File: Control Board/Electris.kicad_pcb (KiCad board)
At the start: 2 copper layers, 57 parts, among them J1 Barrel_Jack, J2 CTRL_ICSP, J3 GFX_ICSP, J4 VGA, Q1 MMBT2222ALT3G, SW1 SW_ML, SW2 SW_MR, SW3 SW_TL, SW4 SW_TR, SW5 SW_DS, SW6 SW_DH, SW7 SW_HL, U1 ATmega328P-AU, U2 AP1509-50SG-13, U3 ATmega328P-AU, Y1 16MHz, Y2 16MHz

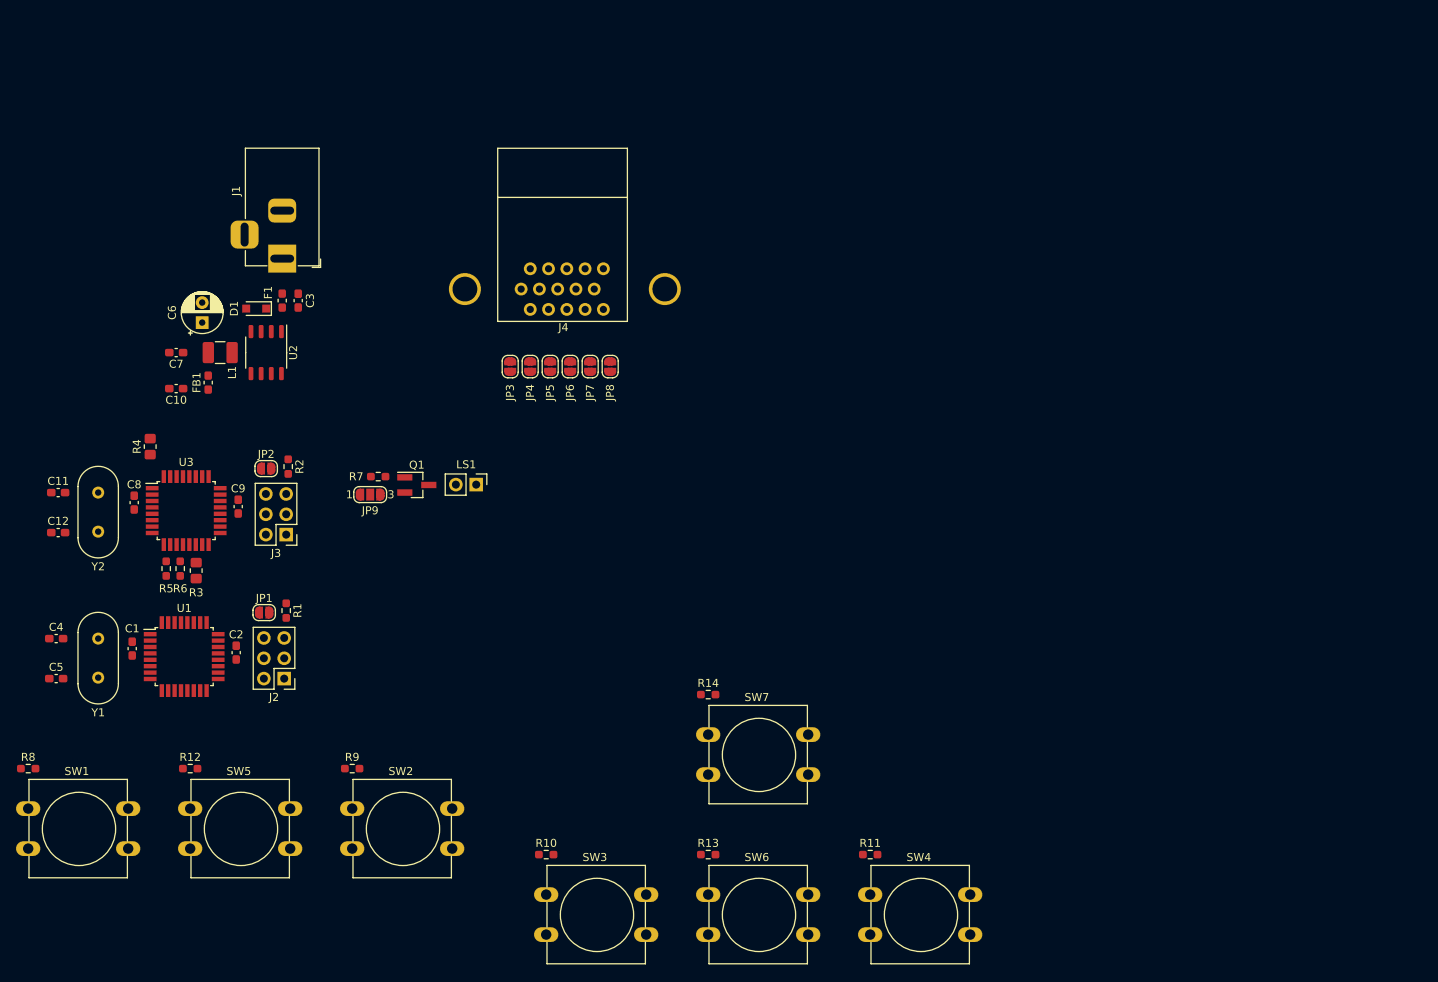
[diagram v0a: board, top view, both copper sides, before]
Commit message: Switched to RP2040, finished schematic, started layout.
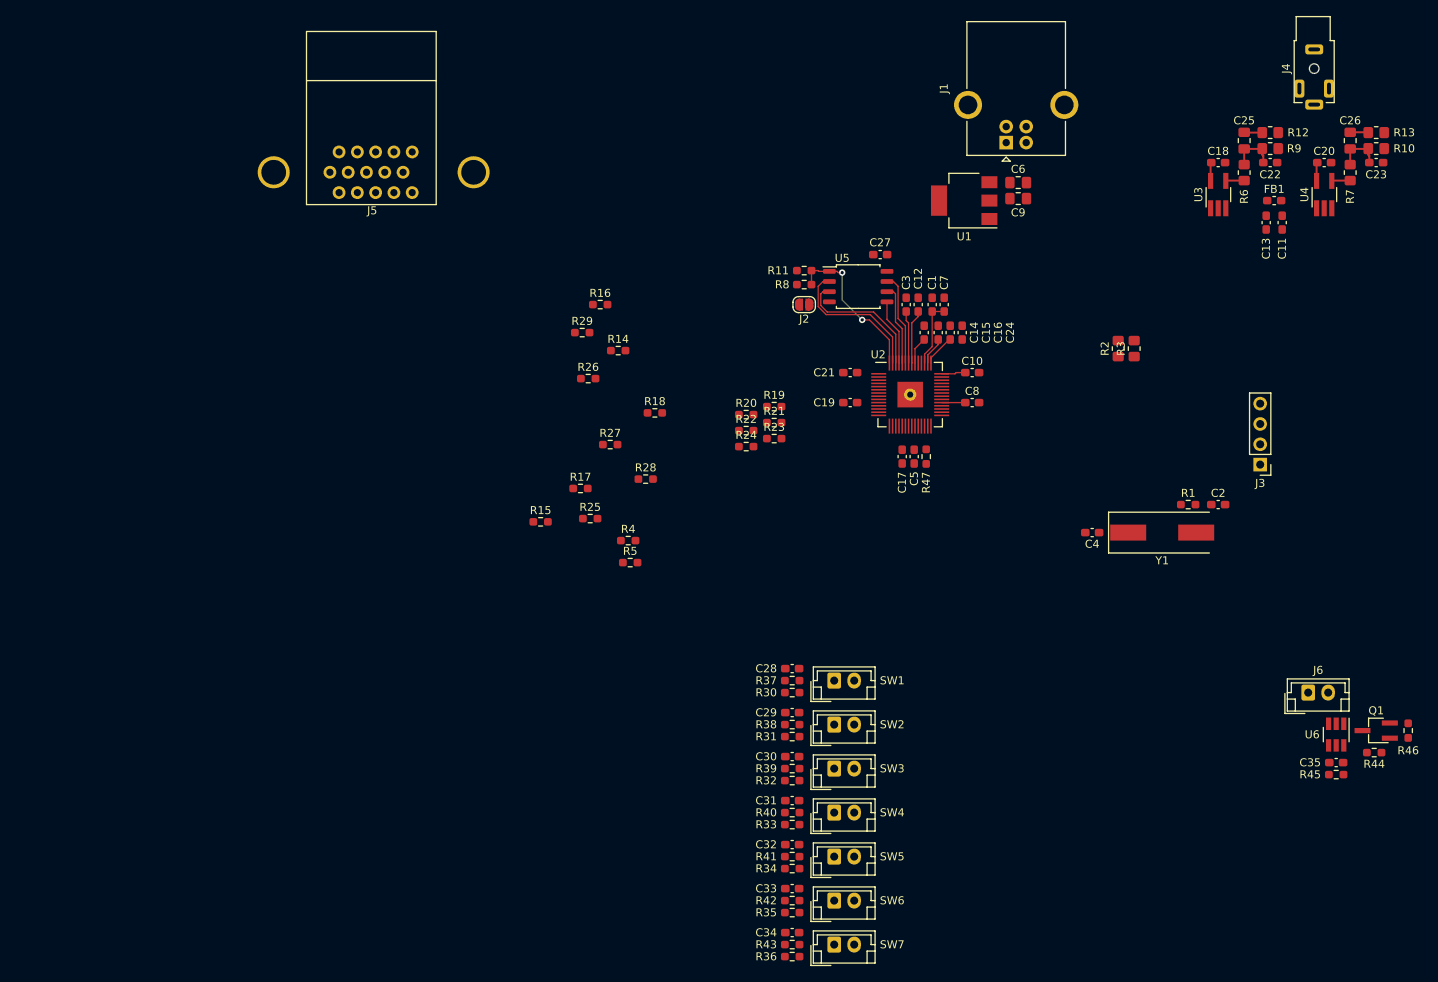
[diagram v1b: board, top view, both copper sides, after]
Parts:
- removed D1: NSR0530HT1G, Diode_SMD:D_SOD-323_HandSoldering
- removed F1: 500mA, Fuse:Fuse_0603_1608Metric_Pad1.05x0.95mm_HandSolder
- removed JP1: CTRL_RST, Jumper:SolderJumper-2_P1.3mm_Open_RoundedPad1.0x1.5mm
- removed JP2: GFX_RST, Jumper:SolderJumper-2_P1.3mm_Open_RoundedPad1.0x1.5mm
- removed JP3: 6R, Jumper:SolderJumper-2_P1.3mm_Open_RoundedPad1.0x1.5mm
- removed JP4: 6G, Jumper:SolderJumper-2_P1.3mm_Open_RoundedPad1.0x1.5mm
- removed JP5: 6B, Jumper:SolderJumper-2_P1.3mm_Open_RoundedPad1.0x1.5mm
- removed JP6: 7R, Jumper:SolderJumper-2_P1.3mm_Open_RoundedPad1.0x1.5mm
- removed JP7: 7G, Jumper:SolderJumper-2_P1.3mm_Open_RoundedPad1.0x1.5mm
- removed JP8: 7B, Jumper:SolderJumper-2_P1.3mm_Open_RoundedPad1.0x1.5mm
- removed JP9: TONE, Jumper:SolderJumper-3_P1.3mm_Open_RoundedPad1.0x1.5mm_NumberLabels
- removed L1: 47uH, Inductor_SMD:L_1210_3225Metric_Pad1.42x2.65mm_HandSolder
- removed LS1: Speaker, Connector_PinHeader_2.54mm:PinHeader_1x02_P2.54mm_Vertical
- removed Y2: 16MHz, Crystal:Crystal_HC49-4H_Vertical
- added C13: 0.1uF, Capacitor_SMD:C_0603_1608Metric_Pad1.08x0.95mm_HandSolder, F.Cu at (230.8, 54.2)
- added C14: 0.1uF, Capacitor_SMD:C_0603_1608Metric_Pad1.08x0.95mm_HandSolder, F.Cu at (188.0, 68.0)
- added C15: 0.1uF, Capacitor_SMD:C_0603_1608Metric_Pad1.08x0.95mm_HandSolder, F.Cu at (189.8, 68.0)
- added C16: 0.1uF, Capacitor_SMD:C_0603_1608Metric_Pad1.08x0.95mm_HandSolder, F.Cu at (191.2, 68.0)
- added C17: 0.1uF, Capacitor_SMD:C_0603_1608Metric_Pad1.08x0.95mm_HandSolder, F.Cu at (185.2, 83.5)
- added C18: 0.1uF, Capacitor_SMD:C_0603_1608Metric_Pad1.08x0.95mm_HandSolder, F.Cu at (224.8, 46.8)
- added C19: 0.1uF, Capacitor_SMD:C_0603_1608Metric_Pad1.08x0.95mm_HandSolder, F.Cu at (178.8, 76.8)
- added C20: 0.1uF, Capacitor_SMD:C_0603_1608Metric_Pad1.08x0.95mm_HandSolder, F.Cu at (238.0, 46.8)
- added C21: 0.1uF, Capacitor_SMD:C_0603_1608Metric_Pad1.08x0.95mm_HandSolder, F.Cu at (178.8, 73.0)
- added C22: 0.1uF, Capacitor_SMD:C_0603_1608Metric_Pad1.08x0.95mm_HandSolder, F.Cu at (231.2, 46.8)
- added C23: 0.1uF, Capacitor_SMD:C_0603_1608Metric_Pad1.08x0.95mm_HandSolder, F.Cu at (244.5, 46.8)
- added C24: 1uF, Capacitor_SMD:C_0603_1608Metric_Pad1.08x0.95mm_HandSolder, F.Cu at (192.8, 68.0)
- added C25: 47uF, Capacitor_SMD:C_0805_2012Metric_Pad1.18x1.45mm_HandSolder, F.Cu at (228.0, 44.0)
- added C26: 47uF, Capacitor_SMD:C_0805_2012Metric_Pad1.18x1.45mm_HandSolder, F.Cu at (241.2, 44.0)
- added C27: 0.1uF, Capacitor_SMD:C_0603_1608Metric_Pad1.08x0.95mm_HandSolder, F.Cu at (182.5, 58.2)
- added C28: 0.1uF, Capacitor_SMD:C_0603_1608Metric_Pad1.08x0.95mm_HandSolder, F.Cu at (171.5, 110.0)
- added C29: 0.1uF, Capacitor_SMD:C_0603_1608Metric_Pad1.08x0.95mm_HandSolder, F.Cu at (171.5, 115.5)
- added C30: 0.1uF, Capacitor_SMD:C_0603_1608Metric_Pad1.08x0.95mm_HandSolder, F.Cu at (171.5, 121.0)
- added C31: 0.1uF, Capacitor_SMD:C_0603_1608Metric_Pad1.08x0.95mm_HandSolder, F.Cu at (171.5, 126.5)
- added C32: 0.1uF, Capacitor_SMD:C_0603_1608Metric_Pad1.08x0.95mm_HandSolder, F.Cu at (171.5, 132.0)
- added C33: 0.1uF, Capacitor_SMD:C_0603_1608Metric_Pad1.08x0.95mm_HandSolder, F.Cu at (171.5, 137.5)
- added C34: 0.1uF, Capacitor_SMD:C_0603_1608Metric_Pad1.08x0.95mm_HandSolder, F.Cu at (171.5, 143.0)
- added C35: 1uF, Capacitor_SMD:C_0603_1608Metric_Pad1.08x0.95mm_HandSolder, F.Cu at (239.5, 121.8)
- added J5: VGA, jlib:Connector_Amphenol_ICD15S13E4GX00LF, F.Cu at (124.0, 50.5)
- added J6: LED_1, Connector_JST:JST_EH_B2B-EH-A_1x02_P2.50mm_Vertical, F.Cu at (236.0, 113.0)
- added R15: 1K, Resistor_SMD:R_0603_1608Metric_Pad0.98x0.95mm_HandSolder, F.Cu at (140.1, 91.7)
- added R16: 2K, Resistor_SMD:R_0603_1608Metric_Pad0.98x0.95mm_HandSolder, F.Cu at (147.5, 64.5)
- added R17: 4.02K, Resistor_SMD:R_0603_1608Metric_Pad0.98x0.95mm_HandSolder, F.Cu at (145.0, 87.5)
- added R18: 8.06K, Resistor_SMD:R_0603_1608Metric_Pad0.98x0.95mm_HandSolder, F.Cu at (154.3, 78.0)
- added R19: 499, Resistor_SMD:R_0603_1608Metric_Pad0.98x0.95mm_HandSolder, F.Cu at (169.2, 77.2)
- added R20: 1K, Resistor_SMD:R_0603_1608Metric_Pad0.98x0.95mm_HandSolder, F.Cu at (165.8, 78.2)
- added R21: 2K, Resistor_SMD:R_0603_1608Metric_Pad0.98x0.95mm_HandSolder, F.Cu at (169.2, 79.2)
- added R22: 4.02K, Resistor_SMD:R_0603_1608Metric_Pad0.98x0.95mm_HandSolder, F.Cu at (165.8, 80.2)
- added R23: 8.06K, Resistor_SMD:R_0603_1608Metric_Pad0.98x0.95mm_HandSolder, F.Cu at (169.2, 81.2)
- added R24: 16K, Resistor_SMD:R_0603_1608Metric_Pad0.98x0.95mm_HandSolder, F.Cu at (165.8, 82.2)
- added R25: 499, Resistor_SMD:R_0603_1608Metric_Pad0.98x0.95mm_HandSolder, F.Cu at (146.2, 91.2)
- added R26: 1K, Resistor_SMD:R_0603_1608Metric_Pad0.98x0.95mm_HandSolder, F.Cu at (146.0, 73.8)
- added R27: 2K, Resistor_SMD:R_0603_1608Metric_Pad0.98x0.95mm_HandSolder, F.Cu at (148.8, 82.0)
- added R28: 4.02K, Resistor_SMD:R_0603_1608Metric_Pad0.98x0.95mm_HandSolder, F.Cu at (153.2, 86.3)
- added R29: 8.06K, Resistor_SMD:R_0603_1608Metric_Pad0.98x0.95mm_HandSolder, F.Cu at (145.2, 68.0)
- added R30: 10K, Resistor_SMD:R_0603_1608Metric_Pad0.98x0.95mm_HandSolder, F.Cu at (171.5, 113.0)
- added R31: 10K, Resistor_SMD:R_0603_1608Metric_Pad0.98x0.95mm_HandSolder, F.Cu at (171.5, 118.5)
- added R32: 10K, Resistor_SMD:R_0603_1608Metric_Pad0.98x0.95mm_HandSolder, F.Cu at (171.5, 124.0)
- added R33: 10K, Resistor_SMD:R_0603_1608Metric_Pad0.98x0.95mm_HandSolder, F.Cu at (171.5, 129.5)
- added R34: 10K, Resistor_SMD:R_0603_1608Metric_Pad0.98x0.95mm_HandSolder, F.Cu at (171.5, 135.0)
- added R35: 10K, Resistor_SMD:R_0603_1608Metric_Pad0.98x0.95mm_HandSolder, F.Cu at (171.5, 140.5)
- added R36: 10K, Resistor_SMD:R_0603_1608Metric_Pad0.98x0.95mm_HandSolder, F.Cu at (171.5, 146.0)
- added R37: 1K, Resistor_SMD:R_0603_1608Metric_Pad0.98x0.95mm_HandSolder, F.Cu at (171.5, 111.5)
- added R38: 1K, Resistor_SMD:R_0603_1608Metric_Pad0.98x0.95mm_HandSolder, F.Cu at (171.5, 117.0)
- added R39: 1K, Resistor_SMD:R_0603_1608Metric_Pad0.98x0.95mm_HandSolder, F.Cu at (171.5, 122.5)
- added R40: 1K, Resistor_SMD:R_0603_1608Metric_Pad0.98x0.95mm_HandSolder, F.Cu at (171.5, 128.0)
- added R41: 1K, Resistor_SMD:R_0603_1608Metric_Pad0.98x0.95mm_HandSolder, F.Cu at (171.5, 133.5)
- added R42: 1K, Resistor_SMD:R_0603_1608Metric_Pad0.98x0.95mm_HandSolder, F.Cu at (171.5, 139.0)
- added R43: 1K, Resistor_SMD:R_0603_1608Metric_Pad0.98x0.95mm_HandSolder, F.Cu at (171.5, 144.5)
- added R44: 1K, Resistor_SMD:R_0603_1608Metric_Pad0.98x0.95mm_HandSolder, F.Cu at (244.2, 120.5)
- added R45: 10K, Resistor_SMD:R_0603_1608Metric_Pad0.98x0.95mm_HandSolder, F.Cu at (239.5, 123.2)
- added R46: 10K, Resistor_SMD:R_0603_1608Metric_Pad0.98x0.95mm_HandSolder, F.Cu at (248.5, 117.8)
- added R47: 10K, Resistor_SMD:R_0603_1608Metric_Pad0.98x0.95mm_HandSolder, F.Cu at (188.2, 83.5)
- added U4: 74LVC1G17, Package_TO_SOT_SMD:TSOT-23-5_HandSoldering, F.Cu at (238.0, 50.8)
- added U5: W25Q128JVS, Package_SO:SOIC-8_5.23x5.23mm_P1.27mm, F.Cu at (179.8, 62.2)
- added U6: BCR401UW6Q, Package_TO_SOT_SMD:SOT-23-6_Handsoldering, F.Cu at (239.5, 118.2)
- C11, C12, C5: value 18pF -> 0.1uF
- C2: value 0.1uF -> 27pF
- C4: value 18pF -> 27pF
- C6: value 47uF -> 10uF; footprint Capacitor_THT:CP_Radial_D5.0mm_P2.50mm -> Capacitor_SMD:C_0805_2012Metric_Pad1.18x1.45mm_HandSolder
- C7: value 0.1uF -> 1uF
- C9: value 0.1uF -> 10uF; footprint Capacitor_SMD:C_0603_1608Metric_Pad1.08x0.95mm_HandSolder -> Capacitor_SMD:C_0805_2012Metric_Pad1.18x1.45mm_HandSolder
- FB1: value Ferrite -> FERRITE
- J1: value Barrel_Jack -> USB; footprint Connector_BarrelJack:BarrelJack_Horizontal -> Connector_USB:USB_B_OST_USB-B1HSxx_Horizontal
- J2: value CTRL_ICSP -> USB_BOOT; footprint Connector_PinHeader_2.54mm:PinHeader_2x03_P2.54mm_Vertical -> Jumper:SolderJumper-2_P1.3mm_Open_RoundedPad1.0x1.5mm
- J3: value GFX_ICSP -> SWD; footprint Connector_PinHeader_2.54mm:PinHeader_2x03_P2.54mm_Vertical -> Connector_PinHeader_2.54mm:PinHeader_1x04_P2.54mm_Vertical
- J4: value VGA -> AUDIO; footprint jlib:Connector_Amphenol_ICD15S13E4GX00LF -> jlib:Connector_CUI_SJ1-2503A
- Q1: footprint Package_TO_SOT_SMD:SOT-23_Handsoldering -> Package_TO_SOT_SMD:TSOT-23_HandSoldering
- R1, R8: value 10K -> 1K
- R10, R9: value 10K -> 100; footprint Resistor_SMD:R_0603_1608Metric_Pad0.98x0.95mm_HandSolder -> Resistor_SMD:R_0805_2012Metric_Pad1.20x1.40mm_HandSolder
- R11: value 10K -> DNP
- R12, R13: value 10K -> 1.8K; footprint Resistor_SMD:R_0603_1608Metric_Pad0.98x0.95mm_HandSolder -> Resistor_SMD:R_0805_2012Metric_Pad1.20x1.40mm_HandSolder
- R14: value 10K -> 499
- R2: value 10K -> 27K; footprint Resistor_SMD:R_0603_1608Metric_Pad0.98x0.95mm_HandSolder -> Resistor_SMD:R_0805_2012Metric_Pad1.20x1.40mm_HandSolder
- R3: value 68 -> 27K
- R4: value 68 -> 47; footprint Resistor_SMD:R_0805_2012Metric_Pad1.20x1.40mm_HandSolder -> Resistor_SMD:R_0603_1608Metric_Pad0.98x0.95mm_HandSolder
- R5: value 470 -> 47
- R6: value 470 -> 220; footprint Resistor_SMD:R_0603_1608Metric_Pad0.98x0.95mm_HandSolder -> Resistor_SMD:R_0805_2012Metric_Pad1.20x1.40mm_HandSolder
- R7: value 1K -> 220; footprint Resistor_SMD:R_0603_1608Metric_Pad0.98x0.95mm_HandSolder -> Resistor_SMD:R_0805_2012Metric_Pad1.20x1.40mm_HandSolder
- SW1, SW2, SW3, SW4, SW5, SW6, SW7: footprint Button_Switch_THT:SW_PUSH-12mm -> Connector_JST:JST_EH_B2B-EH-A_1x02_P2.50mm_Vertical
- U1: value ATmega328P-AU -> NCP1117LP-3.3_SOT223; footprint Package_QFP:TQFP-32_7x7mm_P0.8mm -> Package_TO_SOT_SMD:SOT-223-3_TabPin2
- U2: value AP1509-50SG-13 -> RP2040; footprint Package_SO:SOP-8_3.9x4.9mm_P1.27mm -> jlib:QFN_RP2040
- U3: value ATmega328P-AU -> 74LVC1G17; footprint Package_QFP:TQFP-32_7x7mm_P0.8mm -> Package_TO_SOT_SMD:TSOT-23-5_HandSoldering
- Y1: value 16MHz -> 12MHz; footprint Crystal:Crystal_HC49-4H_Vertical -> Crystal:Crystal_SMD_HC49-SD
- moved C11 156.7 mm to (232.8, 54.2), turned to 270 degrees
- moved R12 156.7 mm to (231.2, 43.0)
- moved R6 141.9 mm to (228.0, 48.0), turned to 270 degrees
- moved R9 138.5 mm to (231.2, 45.0)
- moved R10 136.2 mm to (244.5, 45.0)
- moved FB1 135.2 mm to (231.8, 51.5), turned to 0 degrees
- moved U3 134.9 mm to (224.8, 50.8), turned to 90 degrees
- moved Y1 133.7 mm to (217.8, 93.0), turned to 0 degrees
- moved C4 130.2 mm to (209.0, 93.0), turned to 180 degrees
- moved R7 127.3 mm to (241.2, 48.0), turned to 270 degrees
- moved C2 124.1 mm to (224.8, 89.5), turned to 0 degrees
- moved Q1 123.8 mm to (244.5, 117.8), turned to 180 degrees
- moved R13 123.0 mm to (244.5, 43.0)
- moved J3 122.1 mm to (230.0, 84.5)
- moved R3 120.5 mm to (214.2, 70.0)
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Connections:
- C1 pad 1: +5V -> +1V1
- C10 pad 1: +5V -> +3V3
- C11 pad 1: GND -> +3V3
- C11 pad 2: Net-(C11-Pad2) -> GND
- C12 pad 1: GND -> +3V3
- C12 pad 2: Net-(C12-Pad2) -> GND
- C3 pad 1: +12V -> +1V1
- C4 pad 1: GND -> Net-(C4-Pad1)
- C4 pad 2: Net-(C4-Pad2) -> GND
- C5 pad 1: GND -> +1V1
- C5 pad 2: Net-(C5-Pad2) -> GND
- C7 pad 1: Net-(C6-Pad1) -> +1V1
- C8 pad 1: +5V -> +3V3
- C9 pad 1: Net-(C9-Pad1) -> +3V3
- FB1 pad 1: +5V -> +3.3VA
- FB1 pad 2: Net-(C6-Pad1) -> +3V3
- J1 pad 1: Net-(F1-Pad2) -> Net-(C6-Pad1)
- J1 pad 2: GND -> /USB_D-
- J1 pad 3: (no net) -> /USB_D+
- J2 pad 1: /ICSP_MISO_1 -> GND
- J2 pad 2: +5V -> Net-(J2-Pad2)
- J3 pad 1: /ICSP_MISO_2 -> GND
- J3 pad 2: +5V -> /SWD_CLK
- J3 pad 3: /ICSP_SCK_2 -> /SWD_DATA
- J3 pad 4: /ICSP_MOSI_2 -> +3V3
- R1 pad 1: +5V -> Net-(R1-Pad1)
- R1 pad 2: /nRST_1 -> Net-(C2-Pad1)
- R10 pad 1: /BTN_TL -> Net-(C23-Pad1)
- R11 pad 1: /BTN_TR -> +3V3
- R11 pad 2: GND -> /QSPI_CSn
- R12 pad 1: /BTN_DS -> /AUDIO_L
- R13 pad 1: /BTN_DH -> /AUDIO_R
- R14 pad 1: /BTN_HL -> /VGA_R
- R14 pad 2: GND -> /RGB_R0
- R2 pad 1: +5V -> Net-(R2-Pad1)
- R2 pad 2: /nRST_2 -> /USB_D+
- R3 pad 1: /VGA_VSYNC -> Net-(R3-Pad1)
- R3 pad 2: Net-(R3-Pad2) -> /USB_D-
- R5 pad 1: Net-(JP3-Pad1) -> /VGA_VSYNC
- R6 pad 1: Net-(JP6-Pad1) -> Net-(C22-Pad1)
- R6 pad 2: Net-(R6-Pad2) -> /PWM_BUFF_L
- R7 pad 1: Net-(Q1-Pad1) -> Net-(C23-Pad1)
- R7 pad 2: /TONE -> /PWM_BUFF_R
- R8 pad 1: /BTN_ML -> /QSPI_CSn
- R8 pad 2: GND -> Net-(J2-Pad2)
- R9 pad 1: /BTN_MR -> Net-(C22-Pad1)
- SW1 pad 1: /BTN_ML -> Net-(R37-Pad1)
- SW1 pad 2: +5V -> GND
- SW2 pad 1: /BTN_MR -> Net-(R38-Pad1)
- SW2 pad 2: +5V -> GND
- SW3 pad 1: /BTN_TL -> Net-(R39-Pad1)
- SW3 pad 2: +5V -> GND
- SW4 pad 1: /BTN_TR -> Net-(R40-Pad1)
- SW4 pad 2: +5V -> GND
- SW5 pad 1: /BTN_DS -> Net-(R41-Pad1)
- SW5 pad 2: +5V -> GND
- SW6 pad 1: /BTN_DH -> Net-(R42-Pad1)
- SW6 pad 2: +5V -> GND
- SW7 pad 1: /BTN_HL -> Net-(R43-Pad1)
- SW7 pad 2: +5V -> GND
- U1 pad 1: /BTN_MR -> GND
- U1 pad 2: /BTN_TL -> +3V3
- U1 pad 3: GND -> Net-(C6-Pad1)
- U2 pad 1: +12V -> +3V3
- U2 pad 2: Net-(D1-Pad1) -> /RGB_R0
- U2 pad 3: +5V -> /RGB_R1
- U2 pad 4: GND -> /RGB_R2
- U2 pad 5: GND -> /RGB_R3
- U2 pad 6: GND -> /RGB_R4
- U2 pad 7: GND -> /RGB_G0
- U2 pad 8: GND -> /RGB_G1
- U3 pad 1: Net-(R4-Pad2) -> Net-(U3-Pad1)
- U3 pad 2: Net-(U3-Pad2) -> /PWM_L
- U3 pad 4: +5V -> /PWM_BUFF_L
- U3 pad 5: GND -> +3.3VA
- Y1 pad 1: Net-(C4-Pad2) -> Net-(C4-Pad1)
- Y1 pad 2: Net-(C5-Pad2) -> Net-(C2-Pad1)
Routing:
- net +3V3: track 0.00 -> 23.7 mm
- net /QSPI_CSn: track 0.00 -> 20.0 mm, vias 0 -> 2
- net /QSPI_SD1: track 0.00 -> 18.3 mm
- net /QSPI_SD2: track 0.00 -> 17.1 mm
- net +1V1: track 0.00 -> 14.9 mm
- net /QSPI_SD3: track 0.00 -> 11.6 mm
- net /QSPI_SCK: track 0.00 -> 10.2 mm
- net /QSPI_SD0: track 0.00 -> 8.28 mm
- net Net-(C22-Pad1): track 0.00 -> 6.03 mm
- net Net-(C23-Pad1): track 0.00 -> 6.03 mm
- net +3.3VA: track 0.00 -> 4.65 mm
- net /PWM_BUFF_R: track 0.00 -> 2.32 mm
- net /PWM_BUFF_L: track 0.00 -> 2.32 mm
- net /AUDIO_R: track 0.00 -> 2.27 mm
- net /AUDIO_L: track 0.00 -> 2.27 mm
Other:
- rule trace_min: 0.2 -> 0.125

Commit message: Routing
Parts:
- moved R2 27.1 mm to (186.8, 60.8)
- moved R3 27.1 mm to (188.8, 60.8)
- moved C27 3.34 mm to (179.2, 59.0)
- moved J2 1.82 mm to (171.2, 65.0)
- moved R11 1.82 mm to (171.2, 60.8)
- moved R8 1.82 mm to (171.2, 62.5)
- moved U5 1.82 mm to (178.0, 62.8)
- moved C12 1.77 mm to (185.5, 64.2)
- moved C3 1.77 mm to (184.0, 64.2)
- moved C14 1.52 mm to (186.5, 67.8)
- moved C15 0.79 mm to (189.0, 68.2)
- moved C16 0.79 mm to (190.5, 68.2)
- moved C24 0.79 mm to (192.0, 68.2)
- moved C1 0.25 mm to (189.0, 64.8)
- moved C7 0.25 mm to (190.5, 64.8)
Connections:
- net Net-(R2-Pad1) renamed /D+
- net Net-(R3-Pad1) renamed /D-
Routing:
- net /D-: track 0.00 -> 10.8 mm
- net /D+: track 0.00 -> 10.3 mm
- net Net-(J2-Pad2): track 0.00 -> 2.61 mm
- net /QSPI_CSn: track 20.0 -> 21.5 mm
- net /QSPI_SD1: track 18.3 -> 19.7 mm
- net /QSPI_SD2: track 17.1 -> 18.4 mm
- net +1V1: track 14.9 -> 15.8 mm
- net +3V3: track 23.7 -> 24.3 mm
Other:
- net class Differential added: clearance 0.125, trace_width 0.125, via_dia 0.8, via_drill 0.4

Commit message: Routing
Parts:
- C6, C9, U1: moved to B.Cu
- moved C34 89.5 mm to (202.2, 59.0)
- moved R36 89.5 mm to (202.2, 62.0)
- moved R43 89.5 mm to (202.2, 60.5)
- moved SW7 89.5 mm to (207.5, 60.5)
- moved C35 79.9 mm to (195.5, 55.0)
- moved Q1 79.9 mm to (200.5, 51.0)
- moved R44 79.9 mm to (200.2, 53.8)
- moved R45 79.9 mm to (195.5, 56.5)
- moved R46 79.9 mm to (204.5, 51.0)
- moved U6 79.9 mm to (195.5, 51.5)
- moved C33 79.2 mm to (202.2, 64.5)
- moved R35 79.2 mm to (202.2, 67.5)
- moved R42 79.2 mm to (202.2, 66.0)
- moved SW6 79.2 mm to (207.5, 66.0)
- moved J6 76.4 mm to (188.0, 53.5)
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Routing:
- net +3V3: track 24.3 -> 206.1 mm, vias 0 -> 19
- net /VGA_VSYNC: track 0.00 -> 88.2 mm
- net /VGA_HSYNC: track 0.00 -> 88.0 mm
- net /VGA_B: track 0.00 -> 63.1 mm
- net /VGA_G: track 0.00 -> 58.4 mm
- net /PWM_R: track 0.00 -> 55.8 mm, vias 0 -> 2
- net /USB_D-: track 0.00 -> 45.6 mm, vias 0 -> 1
- net /USB_D+: track 0.00 -> 45.6 mm, vias 0 -> 1
- net /VGA_R: track 0.00 -> 44.3 mm
- net /PWM_L: track 0.00 -> 44.2 mm, vias 0 -> 2
- net /LED_OUT: track 0.00 -> 29.1 mm
- net /BTN_ML: track 0.00 -> 25.6 mm
- net /BTN_HL: track 0.00 -> 25.3 mm
- net Net-(C4-Pad1): track 0.00 -> 21.2 mm
- net /BTN_MR: track 0.00 -> 20.6 mm
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- added copper zone on B.Cu, net GND
- added copper zone on F.Cu, net GND
- added copper zone on B.Cu, net Net-(C6-Pad1)
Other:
- board outline added: 80 x 70 mm
- net class Differential: clearance 0.125 -> 0.2

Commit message: Finish routing
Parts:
- added G***: LOGO, Silkscreen:j_logo, F.Cu at (222.5, 66.5)
- added REF**: MountingHole_4.3mm_M4, MountingHole:MountingHole_4.3mm_M4, F.Cu at (230.0, 94.0)
- added REF**: MountingHole_4.3mm_M4, MountingHole:MountingHole_4.3mm_M4, F.Cu at (185.0, 34.2)
- added REF**: MountingHole_4.3mm_M4, MountingHole:MountingHole_4.3mm_M4, F.Cu at (160.0, 94.0)
- added REF**: MountingHole_4.3mm_M4, MountingHole:MountingHole_4.3mm_M4, F.Cu at (230.0, 34.5)
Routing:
- net +3V3: track 206.1 -> 235.2 mm
- net GND: track 5.10 -> 17.6 mm
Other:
- board text added: "#justiceforsvideo"

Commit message: Board ready for production
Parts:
- removed the G*** at (222.5, 66.5)
- added G***: LOGO, jlib:ElectrisLogo_Copper, F.Cu at (226.2, 74.0)
- added G***: LOGO, jlib:JLOGO_1cm, F.Cu at (211.5, 36.5)
- added G***: LOGO, jlib:JLOGO_1cm, B.Cu at (223.5, 68.8)
- added REF**: OSHW-Logo2_14.6x12mm_SilkScreen, Symbol:OSHW-Logo2_14.6x12mm_SilkScreen, B.Cu at (166.2, 63.2)
- added REF**: ESD-Logo_13.2x12mm_SilkScreen, Symbol:ESD-Logo_13.2x12mm_SilkScreen, B.Cu at (166.5, 75.8)
- R2, R3: value 27K -> 27
- moved REF** 1.00 mm to (184.0, 34.2)
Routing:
- net /VGA_G: track 58.4 -> 59.8 mm
- net /VGA_VSYNC: track 88.2 -> 89.1 mm
- net /VGA_HSYNC: track 88.0 -> 88.7 mm
- net GND: vias 40 -> 44
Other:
- net class Default: clearance 0.2 -> 0.1524
- net class Differential: trace_width 0.125 -> 0.127
- rule trace_clearance: 0.2 -> 0.1524
- rule trace_min: 0.125 -> 0.127
- board text added: "Designed by Jasper Rubin in 2021"
- board text added: "E L E C T R I S"
- board text added: "JKR"
- board text added: "SN:"
